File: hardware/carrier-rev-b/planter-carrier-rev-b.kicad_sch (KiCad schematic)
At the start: 20 parts, among them J1 PROTECTED BATTERY, J2 MOISTURE PROBE, J3 WEACT 1.54 INCH, J4 XIAO BAT LEADS, Q1 AO3401A, U1 Seeed XIAO ESP32-C6 or ESP32-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

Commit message: Rev B carrier: freeze on XIAO ESP32-S3, soldered flat
The socketed C6-or-S3 layout left the XIAO's underside BAT pads to a
flying lead that had to leave the socket tunnel and loop back to J4, and
the module could only sit on headers above the passives. With one chip
the board can use its exact land pattern instead.

- U1 is Seeed's XIAO-ESP32-S3-SMD land pattern, rotated so USB-C stays
  at the bottom edge. The underside BAT+/BAT- pads land on plated pads
  (solder from the back, or reflow); J4 is gone.
- Nothing sits under the module. The S3 uses a U.FL antenna, so the C6
  antenna keep-out is dropped: the XIAO moves left beside J3 and the
  switch, divider and filters use the freed right side and top band.
- Pin map rearranged for the layout (display on the left-row pins, D6/TX
  unconnected); firmware Rev B map and platformio-rev-b.ini follow, and
  the C6 env is removed.
- Generators find KiCad on Linux as well as macOS. check.sh passes on
  KiCad 10.0.7: ERC, DRC and parity clean.

Co-Authored-By: Claude Opus 5.5 <noreply@anthropic.com>
Claude-Session: https://claude.ai/code/session_01Y2pFZDRMef9EECGaLGphfU
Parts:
- removed J4: XIAO BAT LEADS, Connector_PinHeader_2.54mm:PinHeader_1x02_P2.54mm_Vertical, symbol Planter:Conn_01x02
- U1: value Seeed XIAO ESP32-C6 or ESP32-S3 -> Seeed XIAO ESP32-S3; footprint Planter:Seeed_XIAO_Socketed_2x7_P2.54mm -> Planter:Seeed_XIAO_ESP32S3_SMD; symbol Planter:XIAO_C6_S3_Carrier -> Planter:XIAO_ESP32S3_Carrier
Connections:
- net EPD_BUSY: now also U1.5 (D4 IO5); no longer U1.8 (D7/RX C6:IO17 S3:IO44)
- net EPD_CS: now also U1.9 (D8 IO7); no longer U1.4 (D3 C6:IO21 S3:IO4)
- net EPD_DC: now also U1.8 (D7/RX IO44); no longer U1.5 (D4 C6:IO22 S3:IO5)
- net EPD_SCLK: now also U1.10 (D9 IO8); no longer U1.9 (D8/SCK C6:IO19 S3:IO7)
- net GND: now also U1.24 (BAT-)
- net MOIST_ADC: now also U1.3 (D2/A2 IO3); no longer U1.2 (D1/A1 C6:IO1 S3:IO2)
- net PACK+: now also U1.23 (BAT+)
- net PERIPH_EN_N: now also U1.2 (D1 IO2); no longer U1.3 (D2 C6:IO2 S3:IO3)
- net VBAT_ADC: now also U1.4 (D3/A3 IO4); no longer U1.1 (D0/A0 C6:IO0 S3:IO1)
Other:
- note added: "04 XIAO ESP32-S3 (SOLDERED FLAT ON ITS CASTELLATIONS)"
- note added: "BOTH 200k resistors fitted. 4.2V pack -> 2.1V ADC. C1 at U1. The XIAO has no onboard battery divider."
- note added: "Board: 50.12 x 32.60mm, WeAct 1.54-inch module outline and M2.5 hole pattern (44.52 x 27.00mm). The S3 uses an external U.FL antenna. See README.md for stack-up and first-article gates."
- note added: "Captured by pad label; S3 GPIO shown on each pin. VBUS NC: the XIAO USB-C is the only charger. BAT+/BAT-: the XIAO underside pads, on plated pads soldered from the back. D6 = UART0 TX (ROM boot log): left unconnected. D0 spare. Land pattern is the plain XIAO ESP32-S3 (the Plus has more pads)."
- note added: "PLANTER / XIAO ESP32-S3 CARRIER - REV B"
- note removed: "04 XIAO MODULE (SOCKETED, C6 OR S3)"
- note removed: "BOTH 200k resistors fitted. 4.2V pack -> 2.1V ADC. C1 at U1. Neither XIAO has an onboard A0 divider."
- note removed: "Board: 50.12 x 32.60mm, WeAct 1.54-inch module outline and M2.5 hole pattern (44.52 x 27.00mm). Antenna end of the XIAO is over a copper keep-out. See README.md for stack-up and first-article gates."
- note removed: "Captured by pad label. GPIO per chip shown on each pin. VBUS NC: the XIAO USB-C is the only charger. J4: short strain-relieved leads to the XIAO underside BAT+/BAT-. D6 = UART0 TX on both chips, so BUSY moved to D7 (RX). D6/D9 spare: probe at the socketed XIAO castellations."
- note removed: "PLANTER / XIAO C6-S3 CARRIER - REV B"
- title: Planter XIAO C6/S3 carrier -> Planter XIAO ESP32-S3 carrier

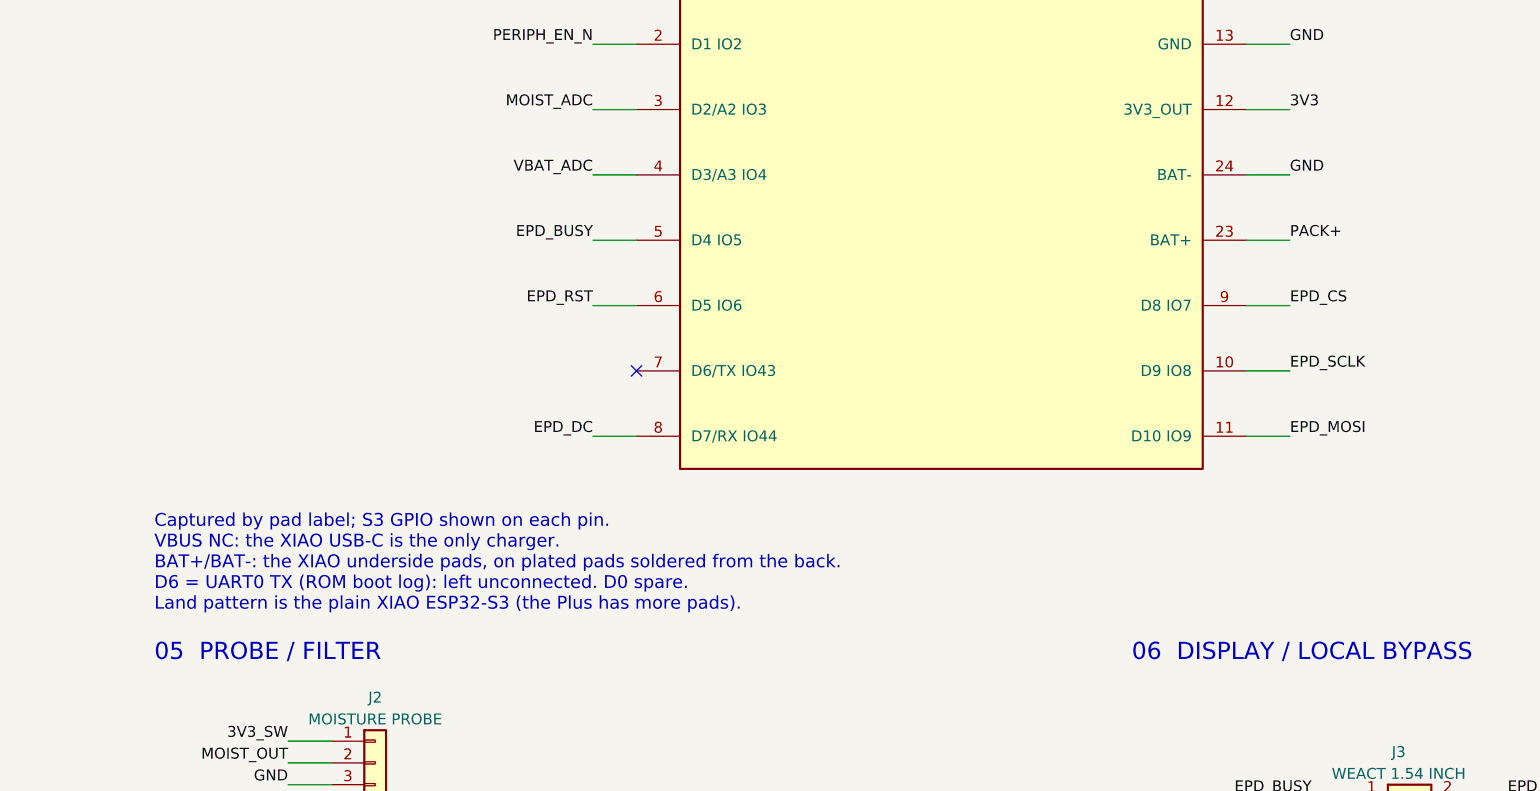
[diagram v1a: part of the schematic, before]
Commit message: Rev B: drop the BAT- pad; return through the GND castellation
The XIAO's underside BAT- pad is module GND, the same net as castellation
13, so a carrier pad under it only added a hidden joint 0.65 mm from BAT+
that could short the cell, and one that is hard to heat on the planes. It
now sits on solder mask and the battery returns through the GND
castellation.

README: the BAT+ pad is plated through, so a stencil puts no paste on it;
it is soldered from the back even when the rest is reflowed. Add a
TP1-to-GND short check and a powered check of the hidden joint.

Co-Authored-By: Claude Opus 5.5 <noreply@anthropic.com>
Claude-Session: https://claude.ai/code/session_01Y2pFZDRMef9EECGaLGphfU
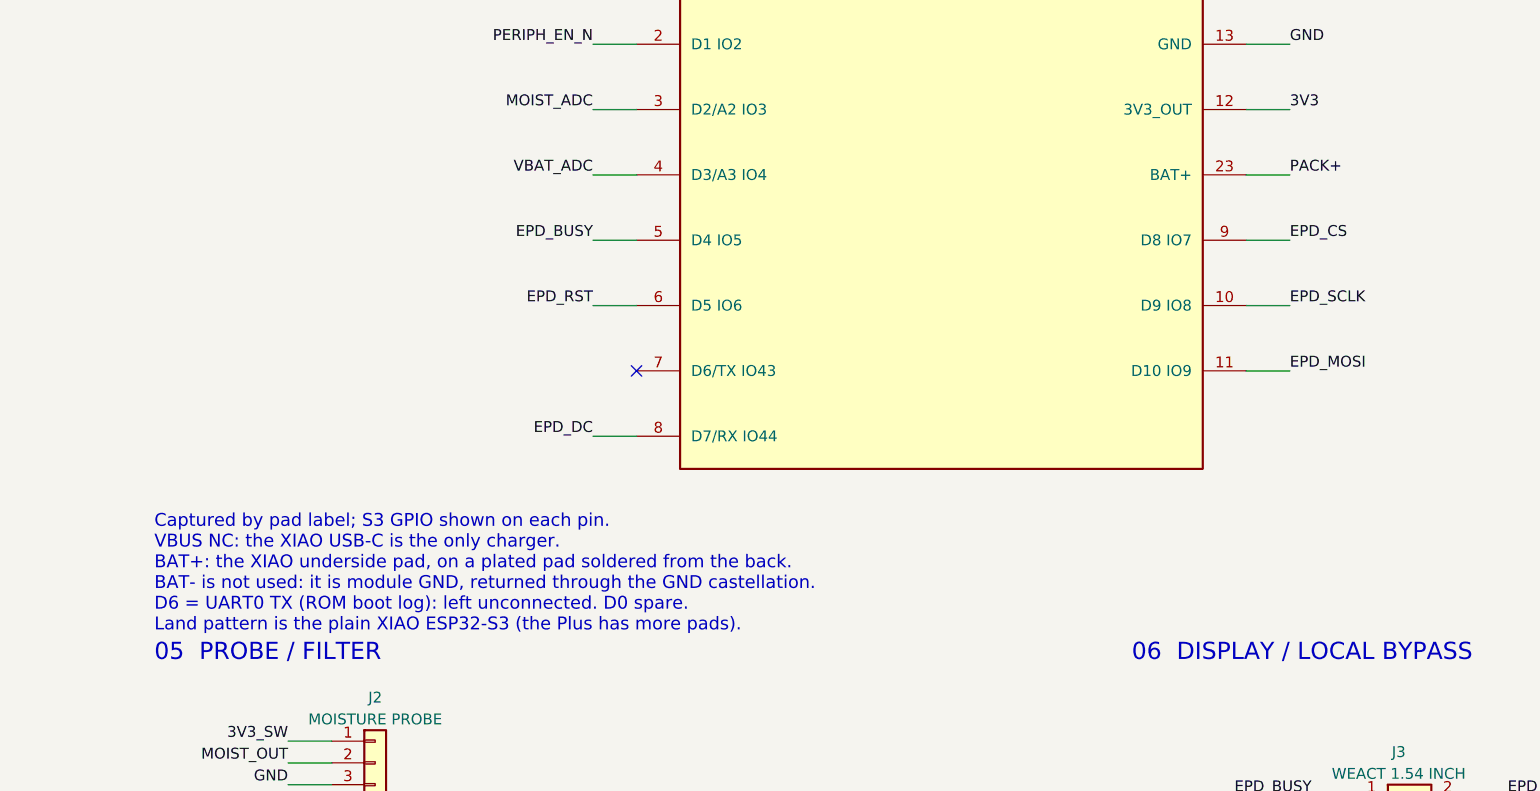
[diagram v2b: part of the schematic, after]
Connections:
- net GND: no longer U1.24 (BAT-)
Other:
- note added: "Captured by pad label; S3 GPIO shown on each pin. VBUS NC: the XIAO USB-C is the only charger. BAT+: the XIAO underside pad, on a plated pad soldered from the back. BAT- is not used: it is module GND, returned through the GND castellation. D6 = UART0 TX (ROM boot log): left unconnected. D0 spare. Land pattern is the plain XIAO ESP32-S3 (the Plus has more pads)."
- note removed: "Captured by pad label; S3 GPIO shown on each pin. VBUS NC: the XIAO USB-C is the only charger. BAT+/BAT-: the XIAO underside pads, on plated pads soldered from the back. D6 = UART0 TX (ROM boot log): left unconnected. D0 spare. Land pattern is the plain XIAO ESP32-S3 (the Plus has more pads)."
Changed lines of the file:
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@@
 (pin "13")
 (pin "12")
-(pin "24")
 (pin "23")
 (pin "9")
@@
 (wire (pts (xy 116.84 53.34) (xy 111.76 53.34)) (stroke (width 0) (type default)))
 (label "PACK+" (at 111.76 53.34 0) (effects (font (size 1.27 1.27)) (justify right bottom)))
-(wire (pts (xy 340.36 80.01) (xy 345.44 80.01)) (stroke (width 0) (type default)))
-(label "PACK+" (at 345.44 80.01 0) (effects (font (size 1.27 1.27)) (justify left bottom)))
+(wire (pts (xy 340.36 72.39) (xy 345.44 72.39)) (stroke (width 0) (type default)))
+(label "PACK+" (at 345.44 72.39 0) (effects (font (size 1.27 1.27)) (justify left bottom)))
 (wire (pts (xy 45.72 105.41) (xy 45.72 100.33)) (stroke (width 0) (type default)))
 (label "PACK+" (at 45.72 100.33 0) (effects (font (size 1.27 1.27)) (justify left bottom)))
@@
 (wire (pts (xy 45.72 53.34) (xy 40.64 53.34)) (stroke (width 0) (type default)))
 (label "GND" (at 40.64 53.34 0) (effects (font (size 1.27 1.27)) (justify right bottom)))
-(wire (pts (xy 340.36 72.39) (xy 345.44 72.39)) (stroke (width 0) (type default)))
-(label "GND" (at 345.44 72.39 0) (effects (font (size 1.27 1.27)) (justify left bottom)))
 (wire (pts (xy 340.36 57.15) (xy 345.44 57.15)) (stroke (width 0) (type default)))
 (label "GND" (at 345.44 57.15 0) (effects (font (size 1.27 1.27)) (justify left bottom)))
@@
 (wire (pts (xy 365.76 147.32) (xy 370.84 147.32)) (stroke (width 0) (type default)))
 (label "EPD_CS" (at 370.84 147.32 0) (effects (font (size 1.27 1.27)) (justify left bottom)))
-(wire (pts (xy 340.36 87.63) (xy 345.44 87.63)) (stroke (width 0) (type default)))
-(label "EPD_CS" (at 345.44 87.63 0) (effects (font (size 1.27 1.27)) (justify left bottom)))
+(wire (pts (xy 340.36 80.01) (xy 345.44 80.01)) (stroke (width 0) (type default)))
+(label "EPD_CS" (at 345.44 80.01 0) (effects (font (size 1.27 1.27)) (justify left bottom)))
 (wire (pts (xy 353.06 149.86) (xy 347.98 149.86)) (stroke (width 0) (type default)))
 (label "EPD_SCLK" (at 347.98 149.86 0) (effects (font (size 1.27 1.27)) (justify right bottom)))
-(wire (pts (xy 340.36 95.25) (xy 345.44 95.25)) (stroke (width 0) (type default)))
-(label "EPD_SCLK" (at 345.44 95.25 0) (effects (font (size 1.27 1.27)) (justify left bottom)))
+(wire (pts (xy 340.36 87.63) (xy 345.44 87.63)) (stroke (width 0) (type default)))
+(label "EPD_SCLK" (at 345.44 87.63 0) (effects (font (size 1.27 1.27)) (justify left bottom)))
 (wire (pts (xy 365.76 149.86) (xy 370.84 149.86)) (stroke (width 0) (type default)))
 (label "EPD_MOSI" (at 370.84 149.86 0) (effects (font (size 1.27 1.27)) (justify left bottom)))
-(wire (pts (xy 340.36 102.87) (xy 345.44 102.87)) (stroke (width 0) (type default)))
-(label "EPD_MOSI" (at 345.44 102.87 0) (effects (font (size 1.27 1.27)) (justify left bottom)))
+(wire (pts (xy 340.36 95.25) (xy 345.44 95.25)) (stroke (width 0) (type default)))
+(label "EPD_MOSI" (at 345.44 95.25 0) (effects (font (size 1.27 1.27)) (justify left bottom)))
 (wire (pts (xy 353.06 152.4) (xy 347.98 152.4)) (stroke (width 0) (type default)))
 (label "GND" (at 347.98 152.4 0) (effects (font (size 1.27 1.27)) (justify right bottom)))
@@
 (text "LOW = on. R1 holds Q1 off at reset. Q1: G=1, S=2, D=3.\nSource is the lower pin here (3V3); drain is 3V3_SW.\nFirmware must not drive an unpowered peripheral high." (at 20 197 0) (effects (font (size 1.5 1.5)) (justify left top)))
 (text "04  XIAO ESP32-S3 (SOLDERED FLAT ON ITS CASTELLATIONS)" (at 213 30 0) (effects (font (size 2 2)) (justify left top)))
-(text "Captured by pad label; S3 GPIO shown on each pin.\nVBUS NC: the XIAO USB-C is the only charger.\nBAT+/BAT-: the XIAO underside pads, on plated pads soldered from the back.\nD6 = UART0 TX (ROM boot log): left unconnected. D0 spare.\nLand pattern is the plain XIAO ESP32-S3 (the Plus has more pads)." (at 213 112 0) (effects (font (size 1.5 1.5)) (justify left top)))
+(text "Captured by pad label; S3 GPIO shown on each pin.\nVBUS NC: the XIAO USB-C is the only charger.\nBAT+: the XIAO underside pad, on a plated pad soldered from the back.\nBAT- is not used: it is module GND, returned through the GND castellation.\nD6 = UART0 TX (ROM boot log): left unconnected. D0 spare.\nLand pattern is the plain XIAO ESP32-S3 (the Plus has more pads)." (at 213 112 0) (effects (font (size 1.5 1.5)) (justify left top)))
 (text "05  PROBE / FILTER" (at 213 127 0) (effects (font (size 2 2)) (justify left top)))
 (text "06  DISPLAY / LOCAL BYPASS" (at 327 127 0) (effects (font (size 2 2)) (justify left top)))
